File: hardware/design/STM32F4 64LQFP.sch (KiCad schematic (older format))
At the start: 17 parts, among them U1 STM32F40X_LQFP64, X2 8MHz 10ppm

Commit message: Some more routing...
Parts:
- CONN2: footprint Socket_Strips:Socket_Strip_Straight_1x05 -> Pads:Pin_Header_Straight_1x05_Pitch1.27mm
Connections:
- net AN_IN: now also U1.10 (PC2(ADC123_IN12)); no longer U1.11 (PC3(ADC123_IN13))
- net FAULTC: now also U1.50 (PA15(JTDI)); no longer U1.28 (PB2-BOOT1)
- net SENSVB: now also U1.11 (PC3(ADC123_IN13)); no longer U1.10 (PC2(ADC123_IN12))
- net THWn: now also U1.28 (PB2-BOOT1); no longer U1.50 (PA15(JTDI))
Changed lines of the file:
@@
 $EndComp
 $Comp
-L GND-RESCUE-BLDC_4 #PWR22
+L GND-RESCUE-BLDC_4 #PWR015
 U 1 1 53F757E9
 P 8250 1600
-F 0 "#PWR22" H 8250 1600 30  0001 C CNN
+F 0 "#PWR015" H 8250 1600 30  0001 C CNN
 F 1 "GND" H 8250 1530 30  0001 C CNN
 F 2 "" H 8250 1600 60  0001 C CNN
@@
 $EndComp
 $Comp
-L GND-RESCUE-BLDC_4 #PWR26
+L GND-RESCUE-BLDC_4 #PWR016
 U 1 1 53F7743B
 P 9100 1650
-F 0 "#PWR26" H 9100 1650 30  0001 C CNN
+F 0 "#PWR016" H 9100 1650 30  0001 C CNN
 F 1 "GND" H 9100 1580 30  0001 C CNN
 F 2 "" H 9100 1650 60  0001 C CNN
@@
 Text HLabel 4500 3150 0    60   Input ~ 0
 SENSCB
-Text HLabel 4500 4850 0    60   Input ~ 0
+Text HLabel 4500 4750 0    60   Input ~ 0
 AN_IN
 Wire Notes Line
@@
 $EndComp
 $Comp
-L GND-RESCUE-BLDC_4 #PWR20
+L GND-RESCUE-BLDC_4 #PWR017
 U 1 1 54097D19
 P 7750 2150
-F 0 "#PWR20" H 7750 2150 30  0001 C CNN
+F 0 "#PWR017" H 7750 2150 30  0001 C CNN
 F 1 "GND" H 7750 2080 30  0001 C CNN
 F 2 "" H 7750 2150 60  0001 C CNN
@@
 I2C_SDA
 $Comp
-L GND #PWR19
+L GND #PWR018
 U 1 1 55E72202
 P 7350 2550
-F 0 "#PWR19" H 7350 2300 50  0001 C CNN
+F 0 "#PWR018" H 7350 2300 50  0001 C CNN
 F 1 "GND" H 7350 2400 50  0000 C CNN
 F 2 "" H 7350 2550 60  0000 C CNN
@@
 $EndComp
 $Comp
-L GND #PWR23
+L GND #PWR019
 U 1 1 55E72244
 P 8400 3300
-F 0 "#PWR23" H 8400 3050 50  0001 C CNN
+F 0 "#PWR019" H 8400 3050 50  0001 C CNN
 F 1 "GND" H 8400 3150 50  0000 C CNN
 F 2 "" H 8400 3300 60  0000 C CNN
@@
 $EndComp
 $Comp
-L GND #PWR27
+L GND #PWR020
 U 1 1 55E72286
 P 9550 2900
-F 0 "#PWR27" H 9550 2650 50  0001 C CNN
+F 0 "#PWR020" H 9550 2650 50  0001 C CNN
 F 1 "GND" H 9550 2750 50  0000 C CNN
 F 2 "" H 9550 2900 60  0000 C CNN
@@
 $EndComp
 $Comp
-L GND #PWR18
+L GND #PWR021
 U 1 1 55E72368
 P 7200 5150
-F 0 "#PWR18" H 7200 4900 50  0001 C CNN
+F 0 "#PWR021" H 7200 4900 50  0001 C CNN
 F 1 "GND" H 7200 5000 50  0000 C CNN
 F 2 "" H 7200 5150 60  0000 C CNN
@@
 $EndComp
 $Comp
-L GND #PWR21
+L GND #PWR022
 U 1 1 55E723AA
 P 8000 6050
-F 0 "#PWR21" H 8000 5800 50  0001 C CNN
+F 0 "#PWR022" H 8000 5800 50  0001 C CNN
 F 1 "GND" H 8000 5900 50  0000 C CNN
 F 2 "" H 8000 6050 60  0000 C CNN
@@
 Text Notes 2100 2150 0    60   ~ 0
 SENSVY1 multi-purpose machen:\n1. Virtueller Sternpunkt.\n2. Pad fuer richtigen Sternpunkt machen.\n3. V_Batt-Messung
-Text HLabel 7500 3200 2    60   3State ~ 0
-THWn
 Text HLabel 8750 2450 2    60   3State ~ 0
+THWn
+Text HLabel 7500 3200 2    60   3State ~ 0
 FAULTC
 Text HLabel 4500 4050 0    60   Output ~ 0
 ZCD_EN
 $Comp
-L +3.3V #PWR17
+L +3.3V #PWR023
 U 1 1 56A5C67D
 P 7200 4200
-F 0 "#PWR17" H 7200 4050 50  0001 C CNN
+F 0 "#PWR023" H 7200 4050 50  0001 C CNN
 F 1 "+3.3V" H 7218 4374 50  0000 C CNN
 F 2 "" H 7200 4200 50  0000 C CNN
@@
 $EndComp
 $Comp
-L +3.3V #PWR16
+L +3.3V #PWR024
 U 1 1 56A5C727
 P 7000 5450
-F 0 "#PWR16" H 7000 5300 50  0001 C CNN
+F 0 "#PWR024" H 7000 5300 50  0001 C CNN
 F 1 "+3.3V" H 7018 5624 50  0000 C CNN
 F 2 "" H 7000 5450 50  0000 C CNN
@@
 $EndComp
 $Comp
-L +3.3V #PWR24
+L +3.3V #PWR025
 U 1 1 56A5C76F
 P 8500 5050
-F 0 "#PWR24" H 8500 4900 50  0001 C CNN
+F 0 "#PWR025" H 8500 4900 50  0001 C CNN
 F 1 "+3.3V" H 8518 5224 50  0000 C CNN
 F 2 "" H 8500 5050 50  0000 C CNN
@@
 F 0 "CONN2" H 10177 3038 50  0000 L CNN
 F 1 "CONN_01X05" H 10177 2946 50  0000 L CNN
-F 2 "Socket_Strips:Socket_Strip_Straight_1x05" H 10100 3000 50  0001 C CNN
+F 2 "Pads:Pin_Header_Straight_1x05_Pitch1.27mm" H 10100 3000 50  0001 C CNN
 F 3 "" H 10100 3000 50  0000 C CNN
 	1    10100 3000
@@
 Text Notes 3850 3550 2    60   ~ 0
 I2C alternativ USART1(PB6,PB7)
-Text HLabel 4500 4750 0    60   Input ~ 0
+Text HLabel 4500 4850 0    60   Input ~ 0
 SENSVB
 Text Notes 3850 4900 2    60   ~ 0
@@
 	7050 2350 7050 2550
 $Comp
-L +3.3V #PWR25
+L +3.3V #PWR026
 U 1 1 56A683FD
 P 9100 950
-F 0 "#PWR25" H 9100 800 50  0001 C CNN
+F 0 "#PWR026" H 9100 800 50  0001 C CNN
 F 1 "+3.3V" H 9118 1124 50  0000 C CNN
 F 2 "" H 9100 950 50  0000 C CNN

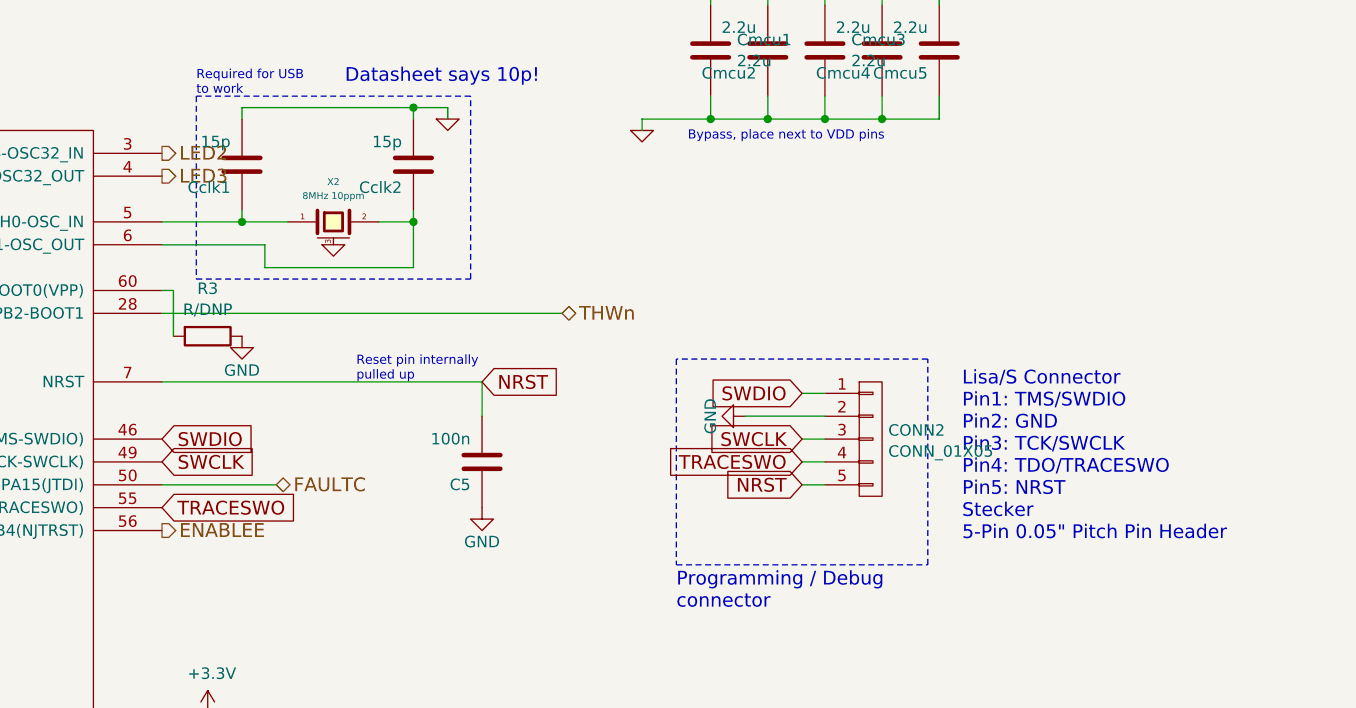
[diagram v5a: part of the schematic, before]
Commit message: Changed pin for LED3
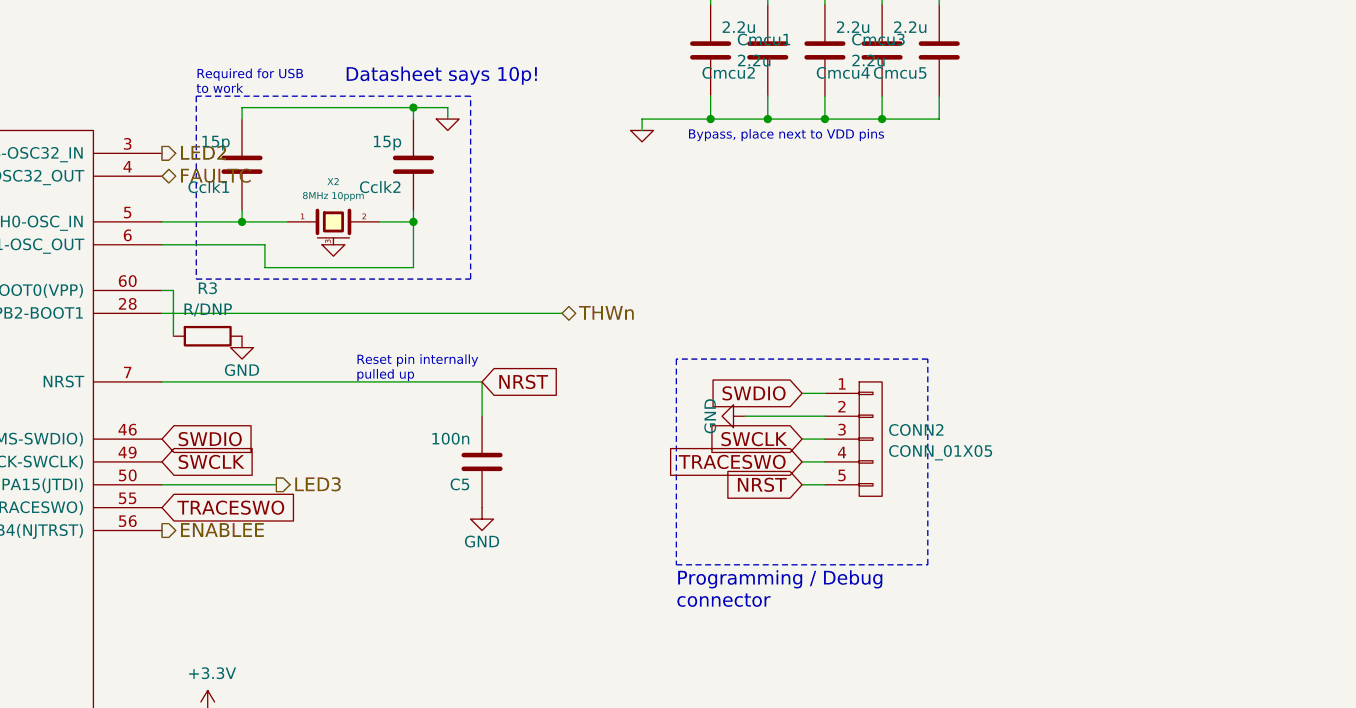
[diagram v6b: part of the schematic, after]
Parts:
- R4: footprint Resistors_SMD:R_0603_HandSoldering -> Resistors_SMD:R_0805
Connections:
- net FAULTC: now also U1.4 (PC15-OSC32_OUT); no longer U1.50 (PA15(JTDI))
- net LED3: now also U1.50 (PA15(JTDI)); no longer U1.4 (PC15-OSC32_OUT)
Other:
- note removed: "Lisa/S Connector\nPin1: TMS/SWDIO\nPin2: GND\nPin3: TCK/SWCLK\nPin4: TDO/TRACESWO\nPin5: NRST\nStecker\n5-Pin 0.05" Pitch Pin Header"
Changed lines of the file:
@@
 F 0 "R4" V 8330 5150 50  0000 C CNN
 F 1 "0R" V 8250 5150 50  0000 C CNN
-F 2 "Resistors_SMD:R_0603_HandSoldering" V 8180 5150 30  0001 C CNN
+F 2 "Resistors_SMD:R_0805" V 8180 5150 30  0001 C CNN
 F 3 "" H 8250 5150 30  0000 C CNN
 	1    8250 5150
@@
 Wire Wire Line
 	8500 5150 8400 5150
-Text Notes 10500 3450 0    60   ~ 0
-Lisa/S Connector\nPin1: TMS/SWDIO\nPin2: GND\nPin3: TCK/SWCLK\nPin4: TDO/TRACESWO\nPin5: NRST\nStecker\n5-Pin 0.05" Pitch Pin Header
 Text HLabel 4500 2150 0    60   Input ~ 0
 SENSVE
@@
 Text HLabel 8750 2450 2    60   3State ~ 0
 THWn
-Text HLabel 7500 3200 2    60   3State ~ 0
+Text HLabel 7000 1850 2    60   3State ~ 0
 FAULTC
 Text HLabel 4500 4050 0    60   Output ~ 0
@@
 Text HLabel 7000 1750 2    60   Output ~ 0
 LED2
-Text HLabel 7000 1850 2    60   Output ~ 0
+Text HLabel 7500 3200 2    60   Output ~ 0
 LED3
 Text HLabel 4500 6050 0    60   Output ~ 0

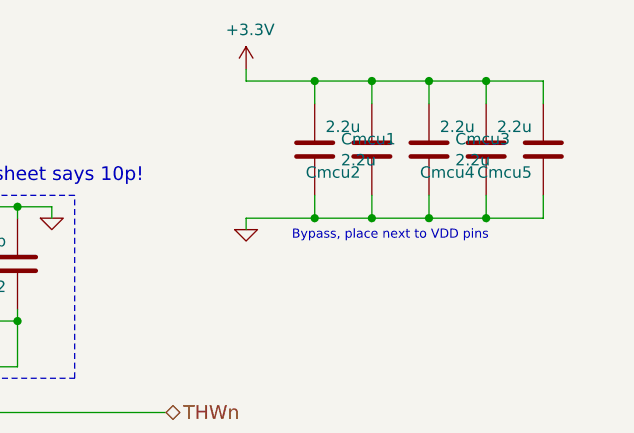
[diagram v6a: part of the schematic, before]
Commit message: Next step: connect GND and PWRGND.
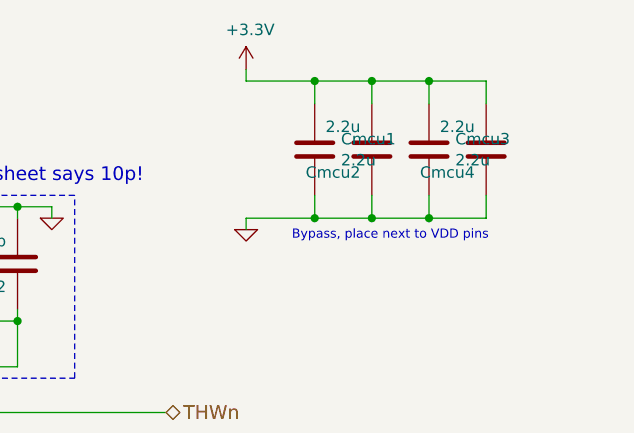
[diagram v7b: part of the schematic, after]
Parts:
- removed Cmcu5: 2.2u, Capacitors_SMD:C_0603, symbol C-RESCUE-BLDC_4
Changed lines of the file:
@@
 $Descr A4 11693 8268
 encoding utf-8
-Sheet 3 11
+Sheet 11 11
 Title "3-Phase Universal Driver"
 Date "2015-08-27"
@@
 $EndComp
 $Comp
-L GND-RESCUE-BLDC_4 #PWR015
+L GND-RESCUE-BLDC_4 #PWR0103
 U 1 1 53F757E9
 P 8250 1600
-F 0 "#PWR015" H 8250 1600 30  0001 C CNN
+F 0 "#PWR0103" H 8250 1600 30  0001 C CNN
 F 1 "GND" H 8250 1530 30  0001 C CNN
 F 2 "" H 8250 1600 60  0001 C CNN
@@
 $EndComp
 $Comp
-L C-RESCUE-BLDC_4 Cmcu5
-U 1 1 53F77434
-P 10400 1300
-F 0 "Cmcu5" H 10450 1400 50  0000 L CNN
-F 1 "2.2u" H 10450 1200 50  0000 L CNN
-F 2 "Capacitors_SMD:C_0603" H 10400 1300 60  0001 C CNN
-F 3 "" H 10400 1300 60  0001 C CNN
-	1    10400 1300
-	-1   0    0    1
-$EndComp
-$Comp
-L GND-RESCUE-BLDC_4 #PWR016
+L GND-RESCUE-BLDC_4 #PWR0104
 U 1 1 53F7743B
 P 9100 1650
-F 0 "#PWR016" H 9100 1650 30  0001 C CNN
+F 0 "#PWR0104" H 9100 1650 30  0001 C CNN
 F 1 "GND" H 9100 1580 30  0001 C CNN
 F 2 "" H 9100 1650 60  0001 C CNN
@@
 	-1   0    0    1
 $EndComp
-Connection ~ 10150 1600
 Wire Wire Line
 	10150 1600 10150 1500
@@
 Wire Wire Line
 	9900 1000 9900 1100
-Connection ~ 10150 1000
 Wire Wire Line
 	10150 1000 10150 1100
 Wire Wire Line
-	10400 1000 10400 1100
-Wire Wire Line
-	9100 1000 10400 1000
-Wire Wire Line
 	9100 950  9100 1000
 Wire Wire Line
-	10400 1600 10400 1500
-Wire Wire Line
-	9100 1600 10400 1600
-Wire Wire Line
 	9100 1650 9100 1600
 Text HLabel 4500 2850 0    60   BiDi ~ 0
@@
 $EndComp
 $Comp
-L GND-RESCUE-BLDC_4 #PWR017
+L GND-RESCUE-BLDC_4 #PWR0105
 U 1 1 54097D19
 P 7750 2150
-F 0 "#PWR017" H 7750 2150 30  0001 C CNN
+F 0 "#PWR0105" H 7750 2150 30  0001 C CNN
 F 1 "GND" H 7750 2080 30  0001 C CNN
 F 2 "" H 7750 2150 60  0001 C CNN
@@
 I2C_SDA
 $Comp
-L GND #PWR018
+L GND #PWR0106
 U 1 1 55E72202
 P 7350 2550
-F 0 "#PWR018" H 7350 2300 50  0001 C CNN
+F 0 "#PWR0106" H 7350 2300 50  0001 C CNN
 F 1 "GND" H 7350 2400 50  0000 C CNN
 F 2 "" H 7350 2550 60  0000 C CNN
@@
 $EndComp
 $Comp
-L GND #PWR019
+L GND #PWR0107
 U 1 1 55E72244
 P 8400 3300
-F 0 "#PWR019" H 8400 3050 50  0001 C CNN
+F 0 "#PWR0107" H 8400 3050 50  0001 C CNN
 F 1 "GND" H 8400 3150 50  0000 C CNN
 F 2 "" H 8400 3300 60  0000 C CNN
@@
 $EndComp
 $Comp
-L GND #PWR020
+L GND #PWR0108
 U 1 1 55E72286
 P 9550 2900
-F 0 "#PWR020" H 9550 2650 50  0001 C CNN
+F 0 "#PWR0108" H 9550 2650 50  0001 C CNN
 F 1 "GND" H 9550 2750 50  0000 C CNN
 F 2 "" H 9550 2900 60  0000 C CNN
@@
 $EndComp
 $Comp
-L GND #PWR021
+L GND #PWR0109
 U 1 1 55E72368
 P 7200 5150
-F 0 "#PWR021" H 7200 4900 50  0001 C CNN
+F 0 "#PWR0109" H 7200 4900 50  0001 C CNN
 F 1 "GND" H 7200 5000 50  0000 C CNN
 F 2 "" H 7200 5150 60  0000 C CNN
@@
 $EndComp
 $Comp
-L GND #PWR022
+L GND #PWR0110
 U 1 1 55E723AA
 P 8000 6050
-F 0 "#PWR022" H 8000 5800 50  0001 C CNN
+F 0 "#PWR0110" H 8000 5800 50  0001 C CNN
 F 1 "GND" H 8000 5900 50  0000 C CNN
 F 2 "" H 8000 6050 60  0000 C CNN
@@
 ZCD_EN
 $Comp
-L +3.3V #PWR023
+L +3.3V #PWR0111
 U 1 1 56A5C67D
 P 7200 4200
-F 0 "#PWR023" H 7200 4050 50  0001 C CNN
+F 0 "#PWR0111" H 7200 4050 50  0001 C CNN
 F 1 "+3.3V" H 7218 4374 50  0000 C CNN
 F 2 "" H 7200 4200 50  0000 C CNN
@@
 $EndComp
 $Comp
-L +3.3V #PWR024
+L +3.3V #PWR0112
 U 1 1 56A5C727
 P 7000 5450
-F 0 "#PWR024" H 7000 5300 50  0001 C CNN
+F 0 "#PWR0112" H 7000 5300 50  0001 C CNN
 F 1 "+3.3V" H 7018 5624 50  0000 C CNN
 F 2 "" H 7000 5450 50  0000 C CNN
@@
 $EndComp
 $Comp
-L +3.3V #PWR025
+L +3.3V #PWR0113
 U 1 1 56A5C76F
 P 8500 5050
-F 0 "#PWR025" H 8500 4900 50  0001 C CNN
+F 0 "#PWR0113" H 8500 4900 50  0001 C CNN
 F 1 "+3.3V" H 8518 5224 50  0000 C CNN
 F 2 "" H 8500 5050 50  0000 C CNN
@@
 	7050 2350 7050 2550
 $Comp
-L +3.3V #PWR026
+L +3.3V #PWR0114
 U 1 1 56A683FD
 P 9100 950
-F 0 "#PWR026" H 9100 800 50  0001 C CNN
+F 0 "#PWR0114" H 9100 800 50  0001 C CNN
 F 1 "+3.3V" H 9118 1124 50  0000 C CNN
 F 2 "" H 9100 950 50  0000 C CNN
@@
 Text Label 4100 3950 0    60   ~ 0
 PWMD
+Wire Wire Line
+	9100 1000 10150 1000
+Wire Wire Line
+	9100 1600 10150 1600
 $EndSCHEMATC

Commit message: Added some part numbers for the BOM
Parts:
- U1: Manufacturer (none) -> ST; Part Number (none) -> STM32F405RGTx
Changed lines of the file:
@@
 F 2 "CRF1:lqfp64_pad_mod" H 5750 3900 60  0001 C CNN
 F 3 "" H 5750 3900 60  0001 C CNN
+F 4 "ST" H 5750 3900 60  0001 C CNN "Manufacturer"
+F 5 "STM32F405RGTx" H 5750 3900 60  0001 C CNN "Part Number"
 	1    5750 3900
 	1    0    0    -1
